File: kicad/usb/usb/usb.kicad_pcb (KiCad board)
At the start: 2 copper layers, 29.4 x 26 mm, 19 parts, among them J1 USB_C_Receptacle_USB2.0_14P, J2 PH1.25mm 2P, J3 Conn_01x07_Pin, Q1 BSS84, SW1 PWR, U1 S-T111B33MC-OGSTFU, U2 MCP73831-2-OT

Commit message: Various kicad edits
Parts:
- J2: value PH1.25mm 2P -> PH2.0mm 2P; footprint Connector_JST:JST_GH_SM02B-GHS-TB_1x02-1MP_P1.25mm_Horizontal -> Connector_JST:JST_PH_S2B-PH-K_1x02_P2.00mm_Horizontal
- SW1: footprint Button_Switch_SMD:SW_SPDT_Shouhan_MSK12C02 -> Button_Switch_THT:SW_Slide_SPDT_Angled_CK_OS102011MA1Q
- moved SW1 9.55 mm to (85.5, 112.3)
- moved R1 8.37 mm to (92.5, 106.1), turned to 90 degrees
- moved C5 8.23 mm to (91.6, 108.4)
- moved C1 7.85 mm to (95.4, 105.5)
- moved C2 7.85 mm to (92.0, 102.5)
- moved C3 7.85 mm to (86.0, 95.9)
- moved C4 7.85 mm to (89.4, 98.8)
- moved J3 7.85 mm to (106.9, 93.3)
- moved R4 7.85 mm to (96.0, 100.3)
- moved R5 7.85 mm to (88.6, 93.3)
- moved R6 7.85 mm to (88.6, 95.7)
- moved U1 7.85 mm to (86.2, 98.8)
- moved U2 7.85 mm to (95.2, 102.5)
- moved J1 7.85 mm to (98.8, 111.5)
- moved Q1 7.85 mm to (86.0, 92.8)
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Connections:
- SW1 pad 1: VSENSE -> unconnected-(SW1-A-Pad1)
- SW1 pad 2: VBAT -> VSENSE
- SW1 pad 3: unconnected-(SW1-C-Pad3) -> VBAT
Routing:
- net SHIELD: track 58.3 -> 34.7 mm
- net VBAT: track 13.3 -> 5.10 mm
- net VSENSE: track 21.0 -> 23.4 mm
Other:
- board size 29.4 x 26 mm -> 31 x 27 mm

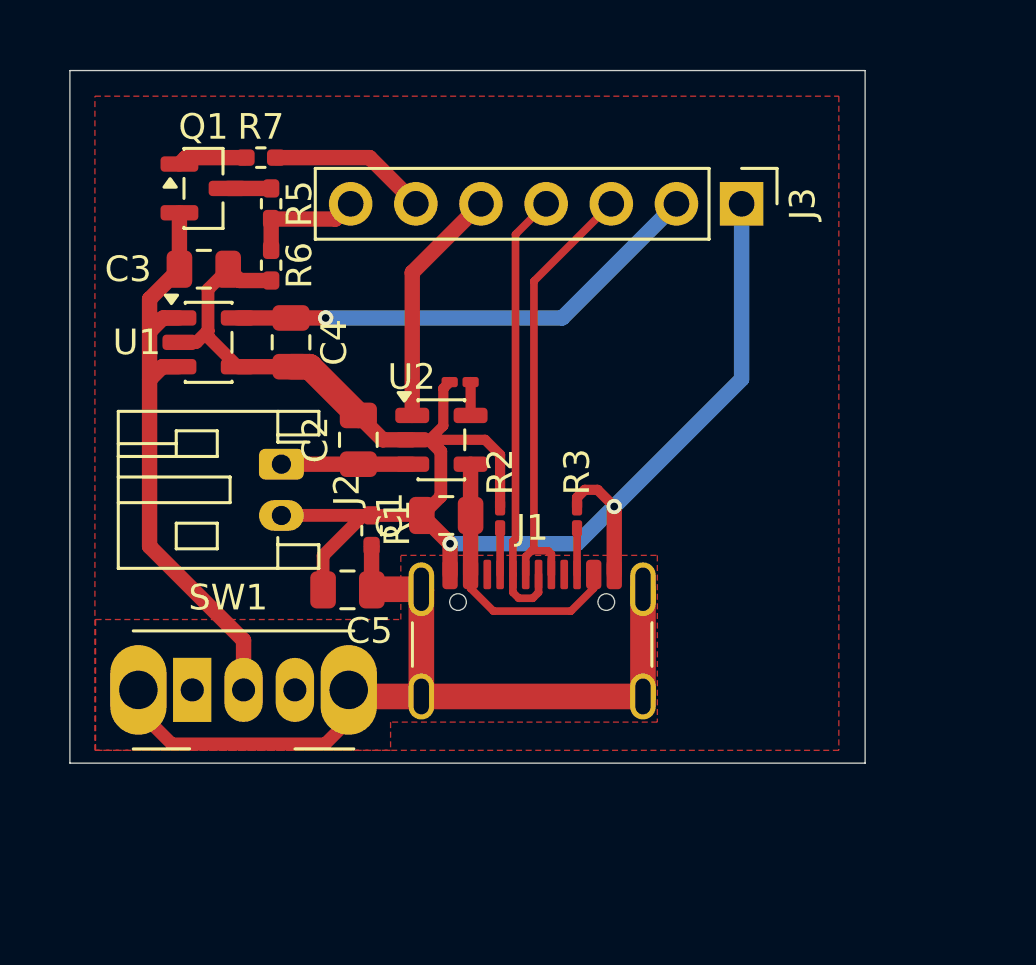
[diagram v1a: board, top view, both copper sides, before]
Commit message: Adjusted parts & traces on usb kicad
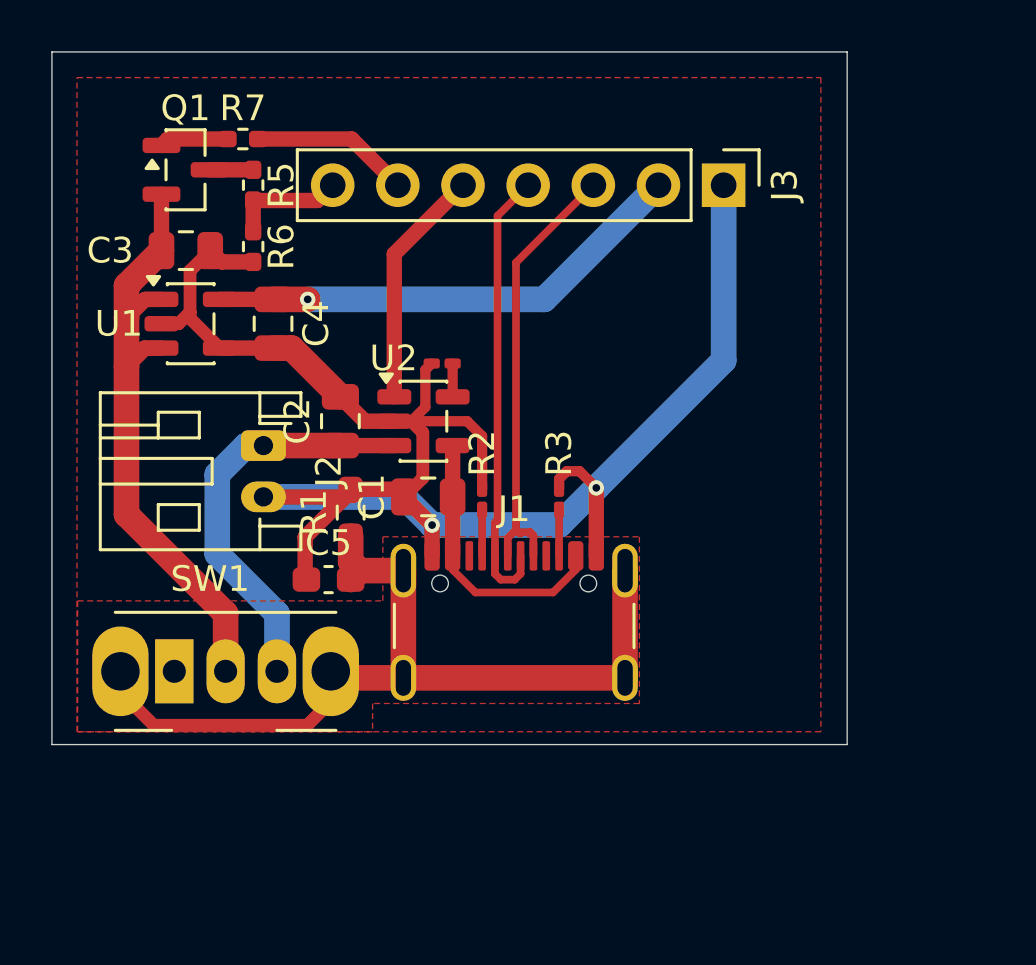
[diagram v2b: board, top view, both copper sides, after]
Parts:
- C5: footprint Capacitor_SMD:C_0805_2012Metric -> Capacitor_SMD:C_0603_1608Metric_Pad1.08x0.95mm_HandSolder
- R1: footprint Resistor_SMD:R_0402_1005Metric_Pad0.72x0.64mm_HandSolder -> Resistor_SMD:R_0603_1608Metric_Pad0.98x0.95mm_HandSolder
- moved R1 1.08 mm to (91.7, 105.4)
- moved J1 1.01 mm to (98.1, 110.8)
- moved C3 1.01 mm to (85.3, 95.2)
- moved R6 1.01 mm to (87.9, 95.0)
- moved C1 1.01 mm to (94.7, 104.8)
- moved C2 1.01 mm to (91.3, 101.8)
- moved C4 1.01 mm to (88.7, 98.0)
- moved J2 1.01 mm to (88.3, 102.8)
- moved J3 1.01 mm to (106.2, 92.6)
- moved Q1 1.01 mm to (85.3, 92.0)
- moved R2 1.01 mm to (96.8, 104.9)
- moved R3 1.01 mm to (99.8, 104.9)
- moved R4 1.01 mm to (95.3, 99.6)
- moved R7 1.01 mm to (87.5, 90.8)
- moved SW1 1.01 mm to (84.8, 111.6)
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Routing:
- net VBAT: track 5.10 -> 16.0 mm
- net GND: track 66.0 -> 73.3 mm
- net VSENSE: track 23.4 -> 24.1 mm
